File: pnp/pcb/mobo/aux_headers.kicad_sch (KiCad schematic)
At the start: 0 parts

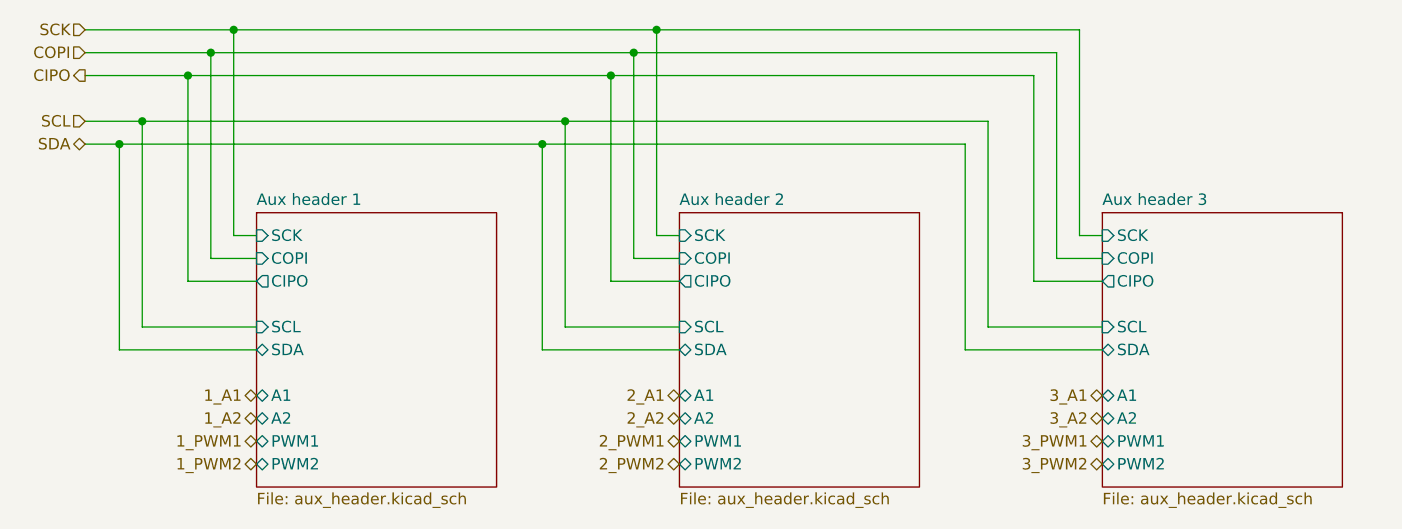
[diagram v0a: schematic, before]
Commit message: Mobo V4A Redesign
Some EMC improvements to schematics.
Reassigned MCU Pins for HW-PWM support.
Changes are still marked with text in the schematics.
Complete PCB Layout reworked
Status: Needs to be verified, and cleaned up a little, but DRC is running green.
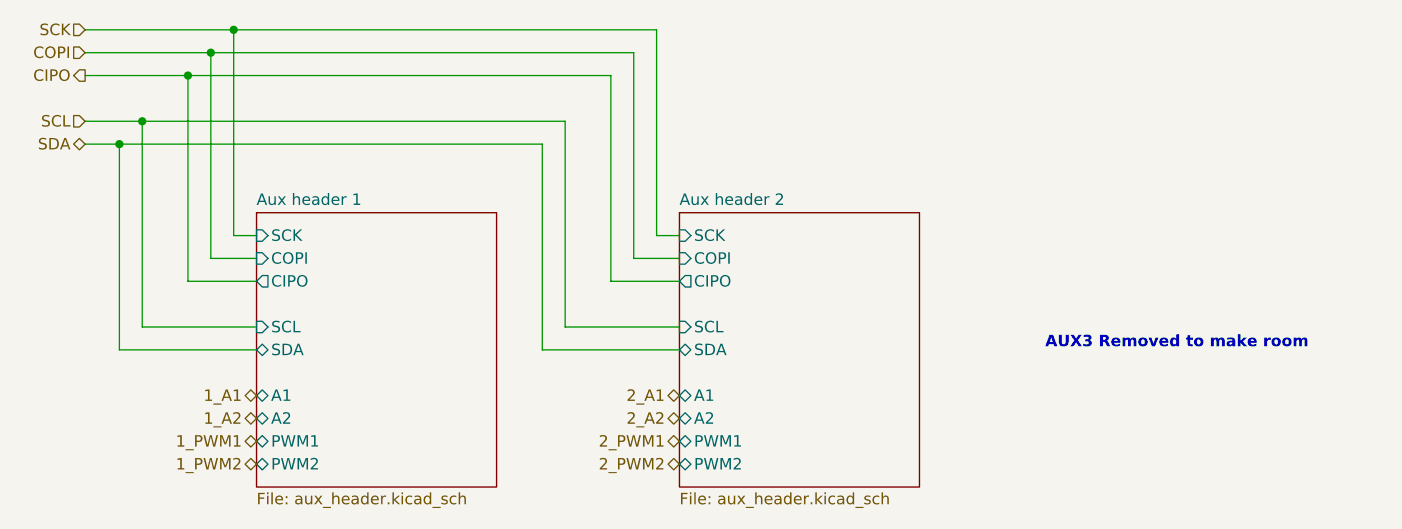
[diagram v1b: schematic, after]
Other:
- removed sheet Aux header 3
- note added: "AUX3 Removed to make room"
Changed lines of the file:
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@@
   (title_block
     (title "LumenPnP Motherboard")
-    (date "2022-03-29")
-    (rev "003")
+    (date "2022-09-09")
+    (rev "004A")
     (company "Opulo")
+    (comment 1 "Reengineered by Magpie")
   )
   (junction (at 85.09 73.66) (diameter 0) (color 0 0 0 0)
   )
-  (junction (at 137.16 68.58) (diameter 0) (color 0 0 0 0)
-  )
   (junction (at 77.47 81.28) (diameter 0) (color 0 0 0 0)
-  )
-  (junction (at 124.46 81.28) (diameter 0) (color 0 0 0 0)
   )
   (junction (at 80.01 78.74) (diameter 0) (color 0 0 0 0)
   )
   (junction (at 87.63 71.12) (diameter 0) (color 0 0 0 0)
-  )
-  (junction (at 132.08 73.66) (diameter 0) (color 0 0 0 0)
-  )
-  (junction (at 134.62 71.12) (diameter 0) (color 0 0 0 0)
-  )
-  (junction (at 127 78.74) (diameter 0) (color 0 0 0 0)
   )
   (junction (at 90.17 68.58) (diameter 0) (color 0 0 0 0)
@@
     (stroke (width 0) (type default) (color 0 0 0 0))
   )
-  (wire (pts (xy 134.62 71.12) (xy 181.61 71.12))
-    (stroke (width 0) (type default) (color 0 0 0 0))
-  )
   (wire (pts (xy 90.17 91.44) (xy 92.71 91.44))
     (stroke (width 0) (type default) (color 0 0 0 0))
@@
     (stroke (width 0) (type default) (color 0 0 0 0))
   )
-  (wire (pts (xy 171.45 104.14) (xy 186.69 104.14))
-    (stroke (width 0) (type default) (color 0 0 0 0))
-  )
   (wire (pts (xy 137.16 91.44) (xy 137.16 68.58))
-    (stroke (width 0) (type default) (color 0 0 0 0))
-  )
-  (wire (pts (xy 127 78.74) (xy 173.99 78.74))
-    (stroke (width 0) (type default) (color 0 0 0 0))
-  )
-  (wire (pts (xy 179.07 96.52) (xy 186.69 96.52))
     (stroke (width 0) (type default) (color 0 0 0 0))
   )
@@
     (stroke (width 0) (type default) (color 0 0 0 0))
   )
-  (wire (pts (xy 184.15 91.44) (xy 184.15 68.58))
-    (stroke (width 0) (type default) (color 0 0 0 0))
-  )
-  (wire (pts (xy 181.61 93.98) (xy 186.69 93.98))
-    (stroke (width 0) (type default) (color 0 0 0 0))
-  )
   (wire (pts (xy 87.63 71.12) (xy 73.66 71.12))
-    (stroke (width 0) (type default) (color 0 0 0 0))
-  )
-  (wire (pts (xy 186.69 101.6) (xy 173.99 101.6))
-    (stroke (width 0) (type default) (color 0 0 0 0))
-  )
-  (wire (pts (xy 173.99 101.6) (xy 173.99 78.74))
     (stroke (width 0) (type default) (color 0 0 0 0))
   )
@@
     (stroke (width 0) (type default) (color 0 0 0 0))
   )
-  (wire (pts (xy 132.08 73.66) (xy 179.07 73.66))
-    (stroke (width 0) (type default) (color 0 0 0 0))
-  )
   (wire (pts (xy 73.66 68.58) (xy 90.17 68.58))
     (stroke (width 0) (type default) (color 0 0 0 0))
@@
   )
   (wire (pts (xy 77.47 81.28) (xy 77.47 104.14))
-    (stroke (width 0) (type default) (color 0 0 0 0))
-  )
-  (wire (pts (xy 124.46 81.28) (xy 171.45 81.28))
     (stroke (width 0) (type default) (color 0 0 0 0))
   )
@@
     (stroke (width 0) (type default) (color 0 0 0 0))
   )
-  (wire (pts (xy 184.15 91.44) (xy 186.69 91.44))
-    (stroke (width 0) (type default) (color 0 0 0 0))
-  )
   (wire (pts (xy 85.09 73.66) (xy 132.08 73.66))
     (stroke (width 0) (type default) (color 0 0 0 0))
@@
     (stroke (width 0) (type default) (color 0 0 0 0))
   )
-  (wire (pts (xy 137.16 68.58) (xy 184.15 68.58))
-    (stroke (width 0) (type default) (color 0 0 0 0))
-  )
   (wire (pts (xy 127 101.6) (xy 127 78.74))
-    (stroke (width 0) (type default) (color 0 0 0 0))
-  )
-  (wire (pts (xy 171.45 81.28) (xy 171.45 104.14))
-    (stroke (width 0) (type default) (color 0 0 0 0))
-  )
-  (wire (pts (xy 179.07 96.52) (xy 179.07 73.66))
     (stroke (width 0) (type default) (color 0 0 0 0))
   )
@@
     (stroke (width 0) (type default) (color 0 0 0 0))
   )
-  (wire (pts (xy 181.61 93.98) (xy 181.61 71.12))
-    (stroke (width 0) (type default) (color 0 0 0 0))
-  )
   (wire (pts (xy 137.16 91.44) (xy 139.7 91.44))
     (stroke (width 0) (type default) (color 0 0 0 0))
@@
   (wire (pts (xy 132.08 96.52) (xy 139.7 96.52))
     (stroke (width 0) (type default) (color 0 0 0 0))
+  )
+  (text "AUX3 Removed to make room" (at 180.34 104.14 0)
+    (effects (font (size 1.27 1.27) bold) (justify left bottom))
   )
   (hierarchical_label "2_PWM1" (shape bidirectional) (at 139.7 114.3 180)
@@
     (effects (font (size 1.27 1.27)) (justify right))
   )
-  (hierarchical_label "3_PWM2" (shape bidirectional) (at 186.69 116.84 180)
-    (effects (font (size 1.27 1.27)) (justify right))
-  )
   (hierarchical_label "1_PWM2" (shape bidirectional) (at 92.71 116.84 180)
-    (effects (font (size 1.27 1.27)) (justify right))
-  )
-  (hierarchical_label "3_PWM1" (shape bidirectional) (at 186.69 114.3 180)
     (effects (font (size 1.27 1.27)) (justify right))
   )
@@
     (effects (font (size 1.27 1.27)) (justify right))
   )
-  (hierarchical_label "3_A2" (shape bidirectional) (at 186.69 111.76 180)
-    (effects (font (size 1.27 1.27)) (justify right))
-  )
   (hierarchical_label "2_PWM2" (shape bidirectional) (at 139.7 116.84 180)
-    (effects (font (size 1.27 1.27)) (justify right))
-  )
-  (hierarchical_label "3_A1" (shape bidirectional) (at 186.69 109.22 180)
     (effects (font (size 1.27 1.27)) (justify right))
   )
@@
       (effects (font (size 1.27 1.27)) (justify left))
     )
-  )
-  (sheet (at 186.69 88.9) (size 26.67 30.48) (fields_autoplaced)
-    (stroke (width 0.1524) (type solid) (color 0 0 0 0))
-    (fill (color 0 0 0 0.0000))
-    (property "Sheet name" "Aux header 3" (id 0) (at 186.69 88.1884 0)
-      (effects (font (size 1.27 1.27)) (justify left bottom))
-    )
-    (property "Sheet file" "aux_header.kicad_sch" (id 1) (at 186.69 119.9646 0)
-      (effects (font (size 1.27 1.27)) (justify left top))
-    )
-    (pin "PWM1" bidirectional (at 186.69 114.3 180)
-      (effects (font (size 1.27 1.27)) (justify left))
-    )
-    (pin "A2" bidirectional (at 186.69 111.76 180)
-      (effects (font (size 1.27 1.27)) (justify left))
-    )
-    (pin "A1" bidirectional (at 186.69 109.22 180)
-      (effects (font (size 1.27 1.27)) (justify left))
-    )
-    (pin "PWM2" bidirectional (at 186.69 116.84 180)
-      (effects (font (size 1.27 1.27)) (justify left))
-    )
-    (pin "COPI" input (at 186.69 93.98 180)
-      (effects (font (size 1.27 1.27)) (justify left))
-    )
-    (pin "CIPO" output (at 186.69 96.52 180)
-      (effects (font (size 1.27 1.27)) (justify left))
-    )
-    (pin "SCL" input (at 186.69 101.6 180)
-      (effects (font (size 1.27 1.27)) (justify left))
-    )
-    (pin "SCK" input (at 186.69 91.44 180)
-      (effects (font (size 1.27 1.27)) (justify left))
-    )
-    (pin "SDA" bidirectional (at 186.69 104.14 180)
-      (effects (font (size 1.27 1.27)) (justify left))
-    )

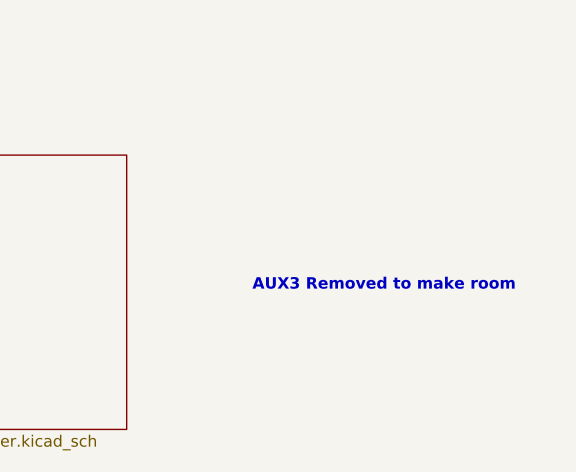
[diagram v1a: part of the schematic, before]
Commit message: Redesign finished
Completed Board redesign and adding more EMC improvements.
Changed all the part numbers to have a Mouser orderable design (except the JST connectors)
All outputs generated
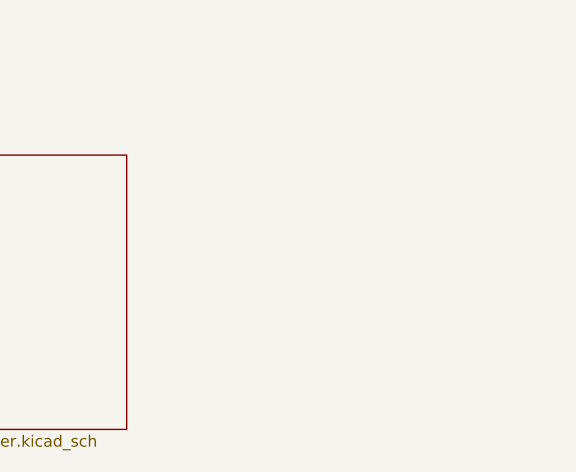
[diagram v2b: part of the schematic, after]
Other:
- note removed: "AUX3 Removed to make room"
- company: Opulo -> Opulo.io
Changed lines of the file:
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@@
   (title_block
     (title "LumenPnP Motherboard")
-    (date "2022-09-09")
-    (rev "004A")
-    (company "Opulo")
+    (date "2022-10-06")
+    (rev "04A")
+    (company "Opulo.io")
     (comment 1 "Reengineered by Magpie")
   )
@@
     (stroke (width 0) (type default) (color 0 0 0 0))
   )
-  (text "AUX3 Removed to make room" (at 180.34 104.14 0)
-    (effects (font (size 1.27 1.27) bold) (justify left bottom))
-  )
   (hierarchical_label "2_PWM1" (shape bidirectional) (at 139.7 114.3 180)
